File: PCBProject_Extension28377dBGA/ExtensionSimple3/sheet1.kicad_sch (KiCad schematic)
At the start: 88 parts, among them J1 Conn_02x05_Odd_Even, J1 Conn_02x08_Top_Bottom, J2 Conn_01x02_Pin, Q1 FMMT618TA, U1 SN74ABT541, U2 SN74ABT541

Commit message: Update ExtensionSimple3 schematic and pcb
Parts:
- added SPI3: Conn_02x04_Counter_Clockwise, Connector_PinSocket_2.54mm:PinSocket_2x04_P2.54mm_Vertical, symbol Connector_Generic:Conn_02x04_Counter_Clockwise
- renumbered SPI1 to SPI-DAC
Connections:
- net AGND: now also SPI-DAC.11, SPI-DAC.9, SPI3.5 (Pin_5), SPI3.6 (Pin_6)
- net D+5V: now also SPI-DAC.10, SPI-DAC.12, SPI3.3 (Pin_3), SPI3.4 (Pin_4)
- net DSP_PWM1_~{FAULT}: now also DSP1.102 (A10_102); no longer DSP1.111 (111_D1)
- net DSP_PWM2_~{FAULT}: now also DSP1.100 (A11_100); no longer DSP1.109 (109_D2)
- net DSP_PWM3_~{FAULT}: now also DSP1.101 (101_D6); no longer DSP1.107 (107_D3)
- net DSP_PWM4_~{FAULT}: now also DSP1.103 (103_D5); no longer DSP1.105 (105_D4)
- net SPI B MI HS: no longer SPI2.2 (Pin_2)
- net SPI B MO HS: no longer SPI2.1 (Pin_1)
- net SPI_A_CK_HS: no longer SPI-DAC.11
- net SPI_A_MI_HS: no longer SPI-DAC.12
- net SPI_A_MO_HS: no longer SPI-DAC.9
- net SPI_B_CK_HS: now also SPI2.7 (Pin_7), SPI3.7 (Pin_7); no longer SPI2.8 (Pin_8)
- net UART_SCI_RXDC: now also DSP1.107 (107_D3); no longer DSP1.135 (135_GP139)
- net UART_SCI_RXDD: now also DSP1.105 (105_D4); no longer DSP1.15 (15_GP141)
- net UART_SCI_TXDC: now also DSP1.106 (A8_106); no longer DSP1.136 (GP140_136)
- net UART_SCI_TXDD: now also DSP1.104 (A9_104); no longer DSP1.16 (GP142_16)
- net ~{SPI_A_STE_HS}: no longer SPI-DAC.10
- net ~{SPI_B_STE_HS}: now also SPI2.8 (Pin_8), SPI3.8 (Pin_8); no longer SPI2.7 (Pin_7)
- net UART_SCI_WRB: now reaches DSP1.123 (123_WE)
- net UART_SCI_WRA: now reaches DSP1.125 (125_RD)
- new net SPI_B_MI_HS: SPI2.2 (Pin_2), SPI3.2 (Pin_2)
- new net SPI_B_MO_HS: SPI2.1 (Pin_1), SPI3.1 (Pin_1)
- new net UART_SCI_WRC: DSP1.109 (109_D2)
- new net UART_SCI_WRD: DSP1.111 (111_D1)
- no-connect marks 86 -> 83
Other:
- note added: "GP104"
- note added: "GP105"
- note added: "GP106"
- note added: "GP107"
- moved on the sheet: C1, C10, C11, C12, C2, C3, C4, C5, C6, C7, C8, C9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

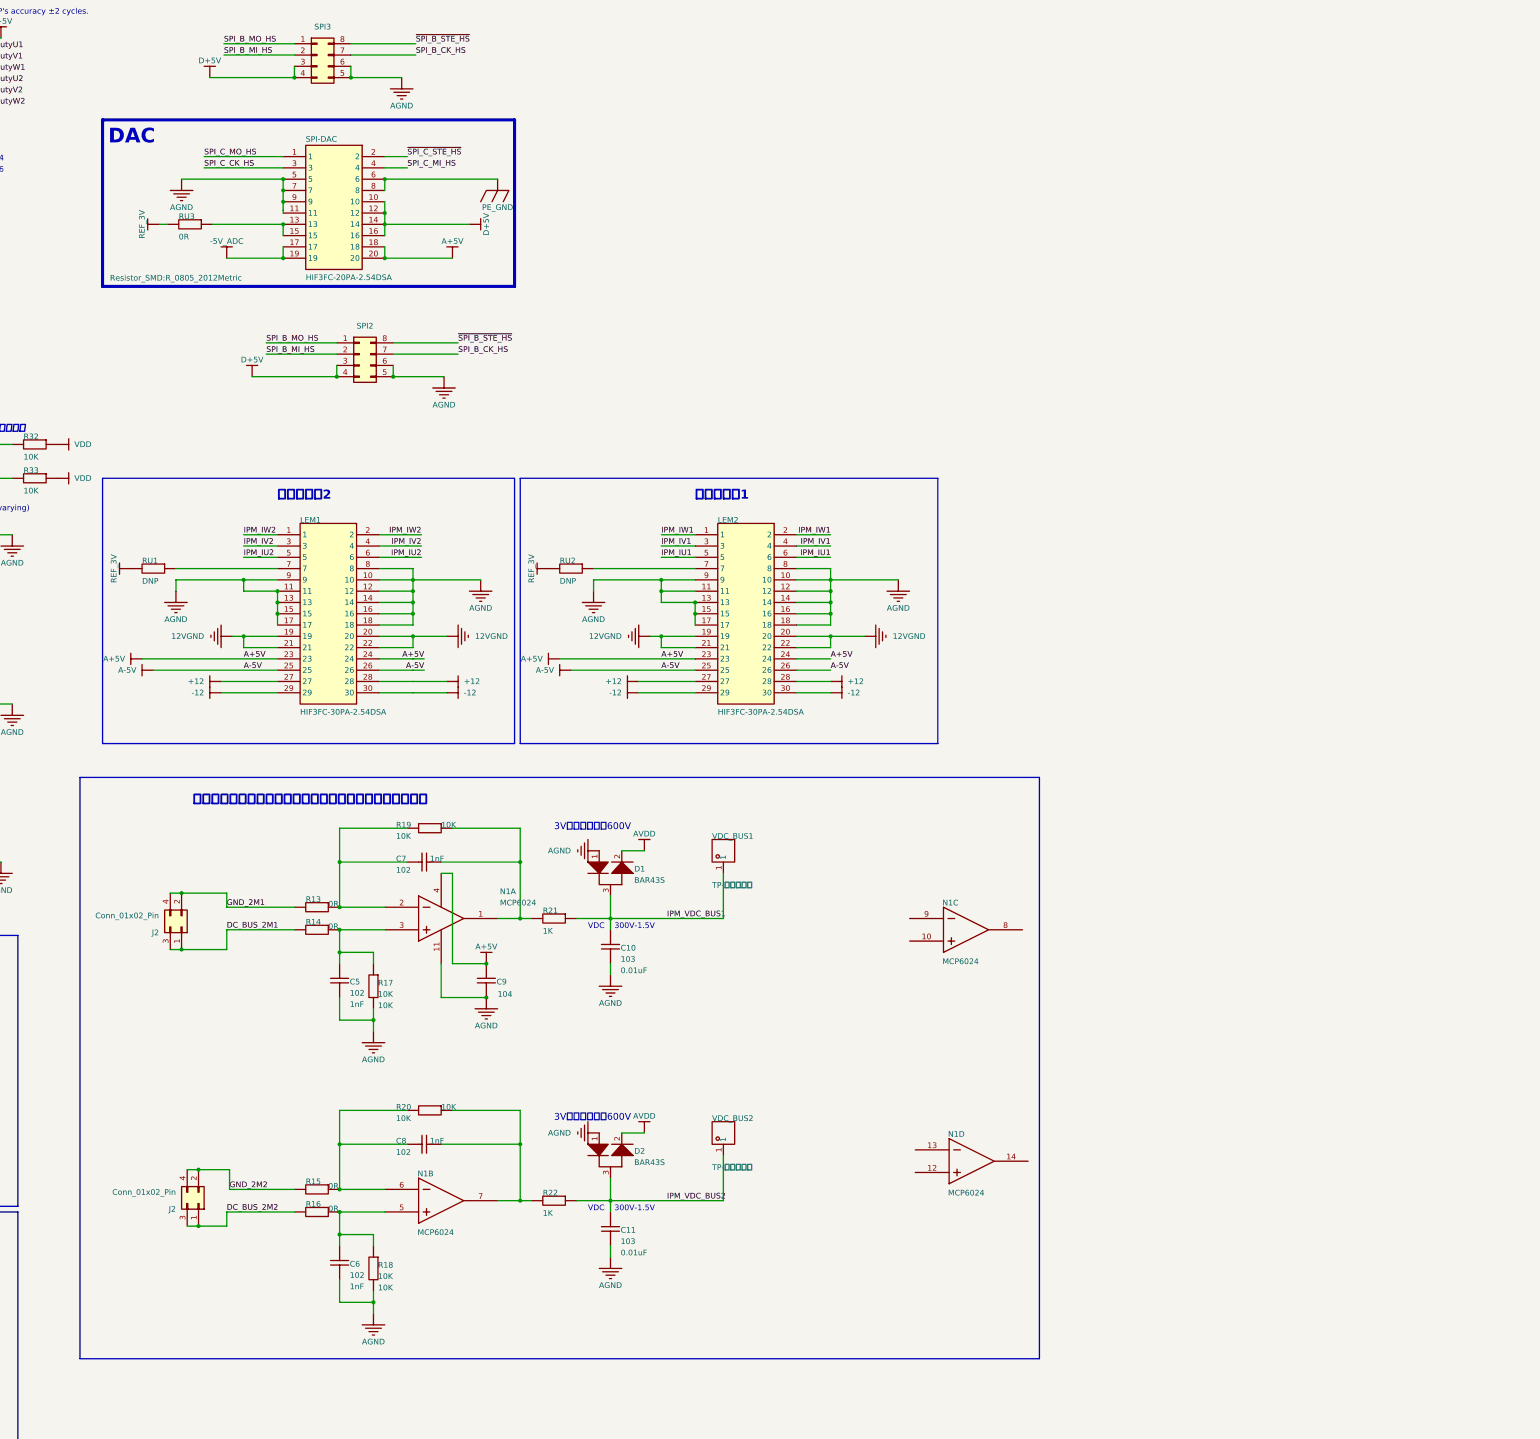
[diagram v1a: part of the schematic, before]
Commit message: finish DACBoard and redefine the pins of DACBoard
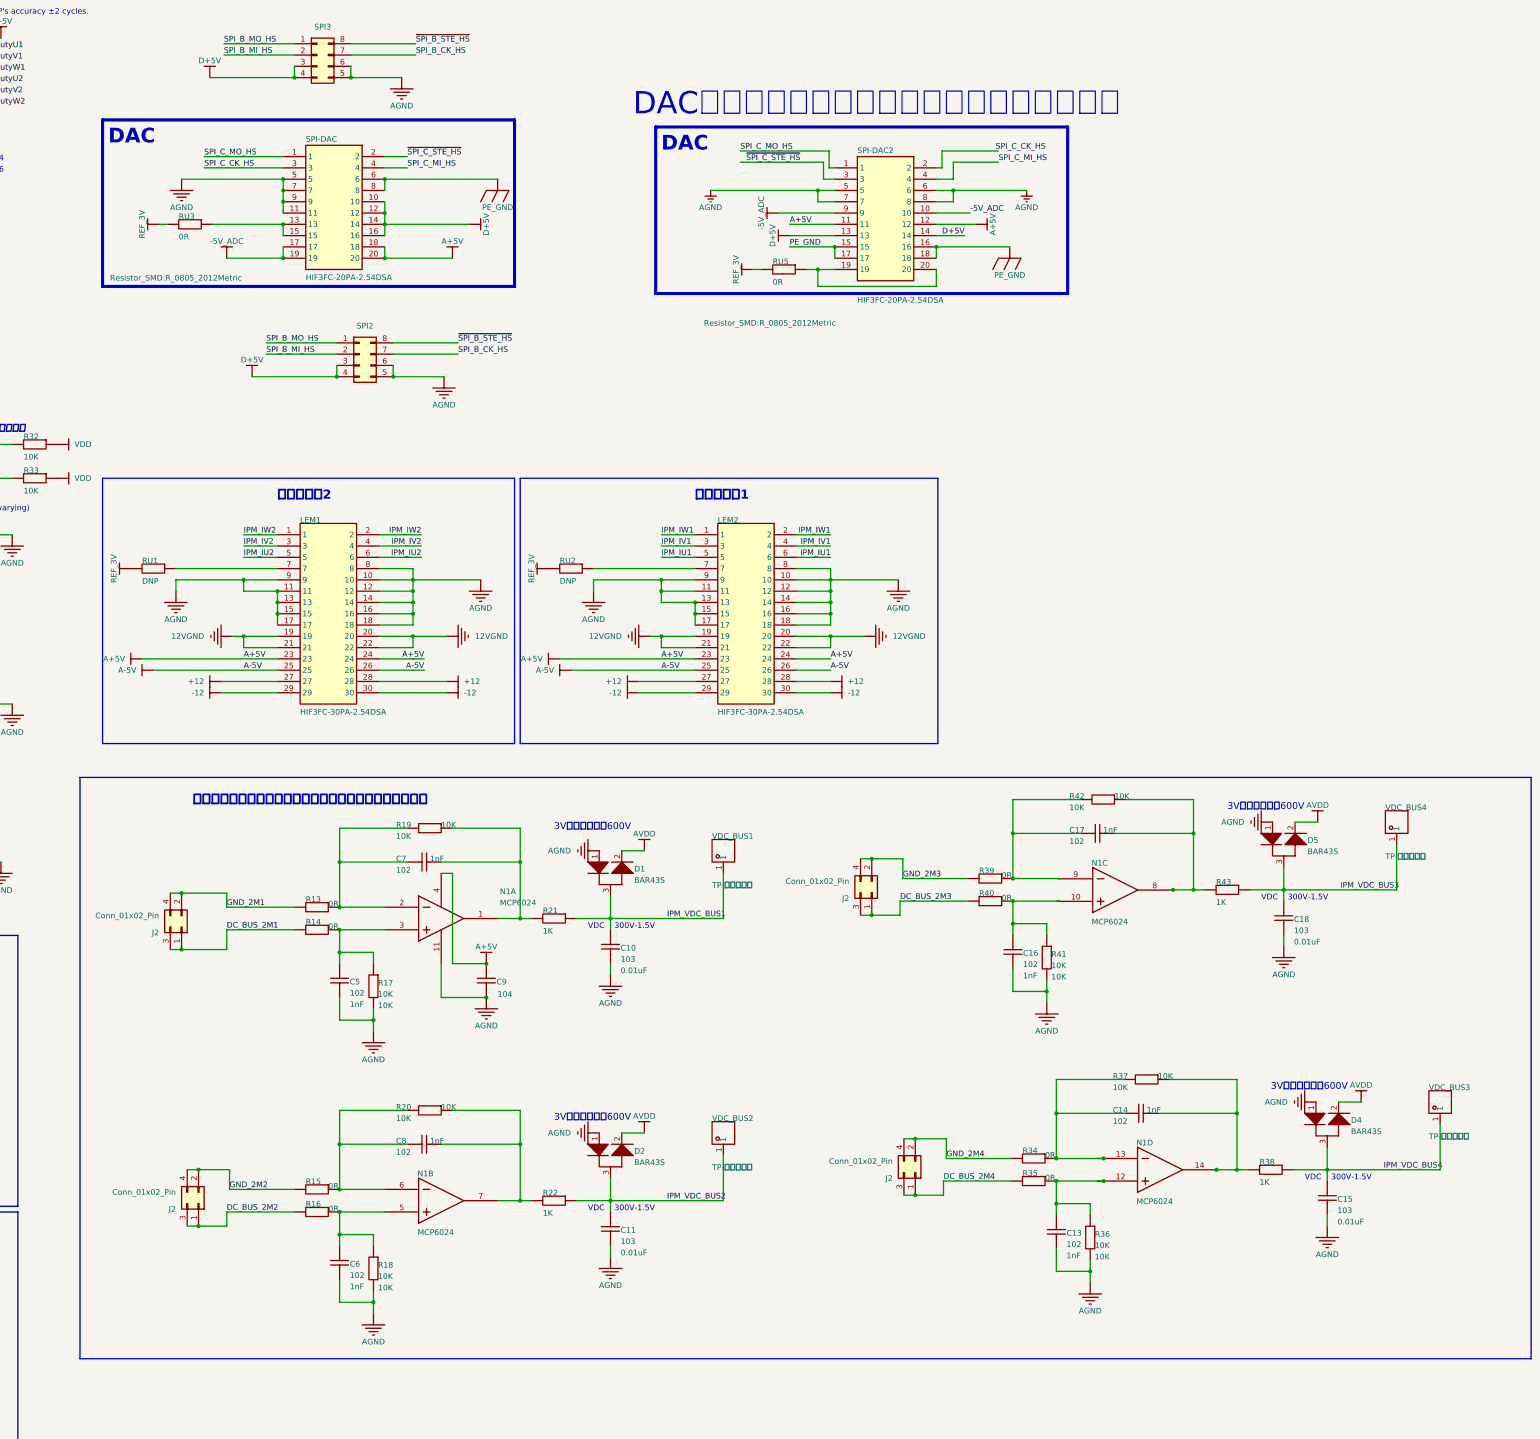
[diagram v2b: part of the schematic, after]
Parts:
- added C13, C16: 102, Capacitor_SMD:C_0805_2012Metric, symbol sheet1-altium-import:root_1_Cap
- added C14, C17: 102, Capacitor_SMD:C_0805_2012Metric, symbol sheet1-altium-import:root_0_Cap
- added C15, C18: 103, Capacitor_SMD:C_0805_2012Metric, symbol sheet1-altium-import:root_1_Cap
- added D4, D5: BAR43S, Package_TO_SOT_SMD:SOT-23, symbol sheet1-altium-import:root_1_BAR43S
- added J2 (x2): Conn_01x02_Pin, Connector_PinSocket_2.54mm:PinSocket_2x02_P2.54mm_Vertical, symbol Connector_Generic:Conn_02x02_Odd_Even
- added R34, R35, R39, R40: 0R, Resistor_SMD:R_0805_2012Metric, symbol sheet1-altium-import:root_2_Res2
- added R36, R41: 10K, Resistor_SMD:R_0805_2012Metric, symbol sheet1-altium-import:root_1_Res2
- added R37, R42: 10K, Resistor_SMD:R_0805_2012Metric, symbol sheet1-altium-import:root_0_Res2
- added R38, R43: 1K, Resistor_SMD:R_0805_2012Metric, symbol sheet1-altium-import:root_0_Res2
- added RU5: 0R, Resistor_SMD:R_0805_2012Metric, symbol sheet1-altium-import:root_0_Res2
- added SPI-DAC2: HIF3FC-20PA-2.54DSA, SamacSys_Parts:SHDR20W56P254_2X10_3290X850X950P, symbol sheet1-altium-import:root_0_HIF3FC-20PA-2.54DSA
- added VDC_BUS3, VDC_BUS4: ${MANUFACTURER PART}, TestPoint:TestPoint_Pad_2.0x2.0mm, symbol sheet1-altium-import:root_1_TP-黄色测试点
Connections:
- net -5V_ADC: now also SPI-DAC2.10, SPI-DAC2.9
- net A+5V: now also SPI-DAC2.11, SPI-DAC2.12
- net AGND: now also C13.1, C15.1, C16.1, C18.1, D4.1, D5.1, R36.1, R41.1
- net AVDD: now also D4.2, D5.2
- net D+5V: now also SPI-DAC2.13, SPI-DAC2.14
- net IPM_VDC_BUS3: now also C18.2, D5.3, R43.2, VDC_BUS4.1
- net IPM_VDC_BUS4: now also C15.2, D4.3, R38.2, VDC_BUS3.1
- net PE_GND: now also SPI-DAC2.15, SPI-DAC2.16, SPI-DAC2.17, SPI-DAC2.18
- net REF_3V: now also RU5.1
- net SPI_C_CK_HS: now also SPI-DAC2.2
- net SPI_C_MI_HS: now also SPI-DAC2.4
- net SPI_C_MO_HS: now also SPI-DAC2.1
- net ~{SPI_C_STE_HS}: now also SPI-DAC2.3
- net at N1.10: now also C16.2, R40.1, R41.2
- net at N1.8: now also C17.2, R42.2, R43.1
- net at N1.9: now also C17.1, R39.1, R42.1
- net at N1.12: now also C13.2, R35.1, R36.2
- net at N1.13: now also C14.1, R34.1, R37.1
- net at N1.14: now also C14.2, R37.2, R38.1
- new net: RU5.2, SPI-DAC2.19, SPI-DAC2.20
- new net DC_BUS_2M3: J2.1 (Pin_1), J2.3 (Pin_3), R40.2
- new net DC_BUS_2M4: J2.1 (Pin_1), J2.3 (Pin_3), R35.2
- new net GNDREF: SPI-DAC2.5, SPI-DAC2.6, SPI-DAC2.7, SPI-DAC2.8
- new net GND_2M3: J2.2 (Pin_2), J2.4 (Pin_4), R39.2
- new net GND_2M4: J2.2 (Pin_2), J2.4 (Pin_4), R34.2
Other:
- note added: "DAC的排针分布选哪个比较好，右边的方便连线"
- moved on the sheet: N1C, N1D

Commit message: finish ExtensionSimple3
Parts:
- removed CAN1, CAN2, UART1, UART2, UART3, UART4: Conn_02x04_Counter_Clockwise, Connector_PinSocket_2.54mm:PinSocket_2x04_P2.54mm_Vertical, symbol Connector_Generic:Conn_02x04_Counter_Clockwise
- removed SPI-DAC: HIF3FC-20PA-2.54DSA, Connector_IDC:IDC-Header_2x10_P2.54mm_Vertical, symbol sheet1-altium-import:root_0_HIF3FC-20PA-2.54DSA
- added CAN_A1, CAN_B1: Conn_01x05, Connector_PinHeader_2.54mm:PinHeader_1x05_P2.54mm_Vertical, symbol Connector_Generic:Conn_01x05
- added R44, R45: 10K, Resistor_SMD:R_0805_2012Metric, symbol sheet1-altium-import:root_2_Res2
- added UART1, UART2, UART3, UART4: Conn_01x06, Connector_PinHeader_2.54mm:PinHeader_1x06_P2.54mm_Vertical, symbol Connector_Generic:Conn_01x06
- R34, R35, R39, R40: value 0R -> 10K
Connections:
- net -5V_ADC is gone; now on net A-5V: SPI-DAC2.10, SPI-DAC2.9
- net D12VGND is gone; now on net 12VGND: J1.13 (Pin_13), J1.13 (Pin_13), J1.15 (Pin_15), J1.15 (Pin_15)
- net DC_BUS_2M3 is gone; now on net AGND: J2.1 (Pin_1), J2.3 (Pin_3), R40.2
- net DC_BUS_2M4 is gone; now on net AGND: J2.1 (Pin_1), J2.3 (Pin_3), R35.2
- net GNDREF is gone; now on net AGND: SPI-DAC2.5, SPI-DAC2.6, SPI-DAC2.7, SPI-DAC2.8
- net +12: now also CAN_A1.1 (Pin_1), CAN_B1.1 (Pin_1)
- net 12VGND: now also RU3.2
- net A+5V: now also R44.1, R45.1
- net AGND: now also RU3.1, CAN_A1.3 (Pin_3), CAN_B1.3 (Pin_3), UART1.3 (Pin_3), UART2.3 (Pin_3), UART3.3 (Pin_3), UART4.3 (Pin_3)
- net D+5V: now also CAN_A1.2 (Pin_2), CAN_B1.2 (Pin_2), UART1.1 (Pin_1), UART2.1 (Pin_1), UART3.1 (Pin_1), UART4.1 (Pin_1)
- net DSP_A_CAN_RX: now also CAN_A1.4 (Pin_4)
- net DSP_A_CAN_TX: now also CAN_A1.5 (Pin_5)
- net DSP_B_CAN_RX: now also CAN_B1.4 (Pin_4)
- net DSP_B_CAN_TX: now also CAN_B1.5 (Pin_5)
- net GND_2M3: now also R45.2
- net GND_2M4: now also R44.2
- net REF_3V: now also UART1.2 (Pin_2), UART2.2 (Pin_2), UART3.2 (Pin_2), UART4.2 (Pin_2); no longer RU3.1
- net UART_SCI_RXDA: now also UART1.4 (Pin_4)
- net UART_SCI_RXDB: now also UART2.4 (Pin_4)
- net UART_SCI_RXDC: now also UART3.4 (Pin_4)
- net UART_SCI_RXDD: now also UART4.4 (Pin_4)
- net UART_SCI_TXDA: now also UART1.6 (Pin_6)
- net UART_SCI_TXDB: now also UART2.6 (Pin_6)
- net UART_SCI_TXDC: now also UART3.6 (Pin_6)
- net UART_SCI_TXDD: now also UART4.6 (Pin_6)
- net UART_SCI_WRA: now also UART1.5 (Pin_5)
- net UART_SCI_WRB: now also UART2.5 (Pin_5)
- net UART_SCI_WRC: now also UART3.5 (Pin_5)
- net UART_SCI_WRD: now also UART4.5 (Pin_5)
- no-connect marks 83 -> 90
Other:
- note removed: "DAC的排针分布选哪个比较好，右边的方便连线"
- moved on the sheet: N1C, N1D, R34, R35, RU5, SPI-DAC2, SPI3

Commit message: @Eorl 1. 需要第二套高速SPI，把 SPI-A 引出来用于DSP之间50MHz通讯。 2. 给I2C找到合适的GPIO引脚，更新原理图 3. 随便找一排GPIO引脚拉到2.54mm的排针上，为INPUT-XBAR预留 4. CAN的12V电源应该是数字电源，现在是用电流传感器的12V，not good 5. CAN排针之间太近，485排针之间太近 6. QEP不需要那个2*10的简牛，删了 7. D12V按原则走外围，不要走DSP下面。
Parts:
- removed C13, C16: 102, Capacitor_SMD:C_0805_2012Metric, symbol sheet1-altium-import:root_1_Cap
- removed C14, C17: 102, Capacitor_SMD:C_0805_2012Metric, symbol sheet1-altium-import:root_0_Cap
- removed C15, C18: 103, Capacitor_SMD:C_0805_2012Metric, symbol sheet1-altium-import:root_1_Cap
- removed CAN_A1, CAN_B1: Conn_01x05, Connector_PinHeader_2.54mm:PinHeader_1x05_P2.54mm_Vertical, symbol Connector_Generic:Conn_01x05
- removed D4, D5: BAR43S, Package_TO_SOT_SMD:SOT-23, symbol sheet1-altium-import:root_1_BAR43S
- removed INC1: HIF3FC-20PA-2.54DSA, Connector_IDC:IDC-Header_2x10_P2.54mm_Vertical, symbol sheet1-altium-import:root_0_HIF3FC-20PA-2.54DSA
- removed J2 (x2): Conn_01x02_Pin, Connector_PinSocket_2.54mm:PinSocket_2x02_P2.54mm_Vertical, symbol Connector_Generic:Conn_02x02_Odd_Even
- removed R34, R35, R39, R40, R44, R45: 10K, Resistor_SMD:R_0805_2012Metric, symbol sheet1-altium-import:root_2_Res2
- removed R36, R41: 10K, Resistor_SMD:R_0805_2012Metric, symbol sheet1-altium-import:root_1_Res2
- removed R37, R42: 10K, Resistor_SMD:R_0805_2012Metric, symbol sheet1-altium-import:root_0_Res2
- removed R38, R43: 1K, Resistor_SMD:R_0805_2012Metric, symbol sheet1-altium-import:root_0_Res2
- removed RU5: 0R, Resistor_SMD:R_0805_2012Metric, symbol sheet1-altium-import:root_0_Res2
- removed SPI-DAC2: HIF3FC-20PA-2.54DSA, SamacSys_Parts:SHDR20W56P254_2X10_3290X850X950P, symbol sheet1-altium-import:root_0_HIF3FC-20PA-2.54DSA
- removed UART1, UART2, UART3, UART4: Conn_01x06, Connector_PinHeader_2.54mm:PinHeader_1x06_P2.54mm_Vertical, symbol Connector_Generic:Conn_01x06
- removed VDC_BUS3, VDC_BUS4: ${MANUFACTURER PART}, TestPoint:TestPoint_Pad_2.0x2.0mm, symbol sheet1-altium-import:root_1_TP-黄色测试点
- added CAN1, CAN2, UART1, UART2, UART3, UART4: Conn_02x04_Counter_Clockwise, Connector_PinSocket_2.54mm:PinSocket_2x04_P2.54mm_Vertical, symbol Connector_Generic:Conn_02x04_Counter_Clockwise
- added SPI-DAC: HIF3FC-20PA-2.54DSA, Connector_IDC:IDC-Header_2x10_P2.54mm_Vertical, symbol sheet1-altium-import:root_0_HIF3FC-20PA-2.54DSA
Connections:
- net 12VGND: no longer J1.13 (Pin_13), J1.13 (Pin_13), J1.15 (Pin_15), J1.15 (Pin_15), RU3.2
- net A+5V: now also SPI-DAC.18, SPI-DAC.20
- net AGND: now also CAN1.5 (Pin_5), CAN1.6 (Pin_6), CAN2.5 (Pin_5), CAN2.6 (Pin_6), SPI-DAC.11, SPI-DAC.5, SPI-DAC.7, SPI-DAC.9, UART1.5 (Pin_5), UART1.6 (Pin_6), UART2.5 (Pin_5), UART2.6 (Pin_6), UART3.5 (Pin_5), UART3.6 (Pin_6), UART4.5 (Pin_5), UART4.6 (Pin_6); no longer RU3.1
- net D+5V: now also CAN1.3 (Pin_3), CAN1.4 (Pin_4), CAN2.3 (Pin_3), CAN2.4 (Pin_4), SPI-DAC.10, SPI-DAC.12, SPI-DAC.14, SPI-DAC.16, UART1.3 (Pin_3), UART1.4 (Pin_4), UART2.3 (Pin_3), UART2.4 (Pin_4), UART3.3 (Pin_3), UART3.4 (Pin_4), UART4.3 (Pin_3), UART4.4 (Pin_4)
- net D12V1: now also UART1.1 (Pin_1), UART1.2 (Pin_2), UART2.1 (Pin_1), UART2.2 (Pin_2), UART3.1 (Pin_1), UART3.2 (Pin_2), UART4.1 (Pin_1), UART4.2 (Pin_2)
- net DSP_A_CAN_RX: now also CAN2.8 (Pin_8)
- net DSP_A_CAN_TX: now also CAN2.7 (Pin_7)
- net DSP_B_CAN_RX: now also CAN1.8 (Pin_8)
- net DSP_B_CAN_TX: now also CAN1.7 (Pin_7)
- net PE_GND: now also SPI-DAC.6, SPI-DAC.8
- net REF_3V: now also RU3.1
- net SPI_C_CK_HS: now also SPI-DAC.3
- net SPI_C_MI_HS: now also SPI-DAC.4
- net SPI_C_MO_HS: now also SPI-DAC.1
- net UART_SCI_RXDA: now also UART1.8 (Pin_8)
- net UART_SCI_RXDB: now also UART2.7 (Pin_7)
- net UART_SCI_RXDC: now also UART3.8 (Pin_8)
- net UART_SCI_RXDD: now also UART4.7 (Pin_7)
- net UART_SCI_TXDA: now also UART1.7 (Pin_7)
- net UART_SCI_TXDB: now also UART2.8 (Pin_8)
- net UART_SCI_TXDC: now also UART3.7 (Pin_7)
- net UART_SCI_TXDD: now also UART4.8 (Pin_8)
- net VDD: now also CAN1.1 (Pin_1), CAN1.2 (Pin_2), CAN2.1 (Pin_1), CAN2.2 (Pin_2)
- net ~{SPI_C_STE_HS}: now also SPI-DAC.2
- new net: RU3.2, SPI-DAC.13, SPI-DAC.15
- new net -5V_ADC: SPI-DAC.17, SPI-DAC.19
- new net D12VGND: J1.13 (Pin_13), J1.13 (Pin_13), J1.15 (Pin_15), J1.15 (Pin_15)
- no-connect marks 90 -> 80
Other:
- moved on the sheet: N1C, N1D, SPI3
